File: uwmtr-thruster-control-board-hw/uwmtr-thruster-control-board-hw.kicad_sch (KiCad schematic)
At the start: 16 parts, among them J1 Conn_01x13_Pin, J2 691137710003, J3 691137710002, U1 TI_MCF8316A

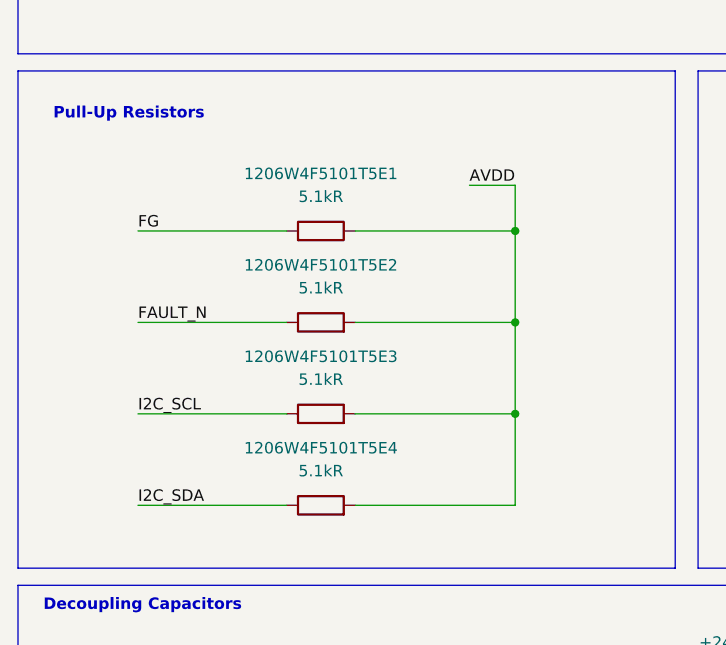
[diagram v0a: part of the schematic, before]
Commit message: Switching resistors to JLCPCB assembly non-extended parts.
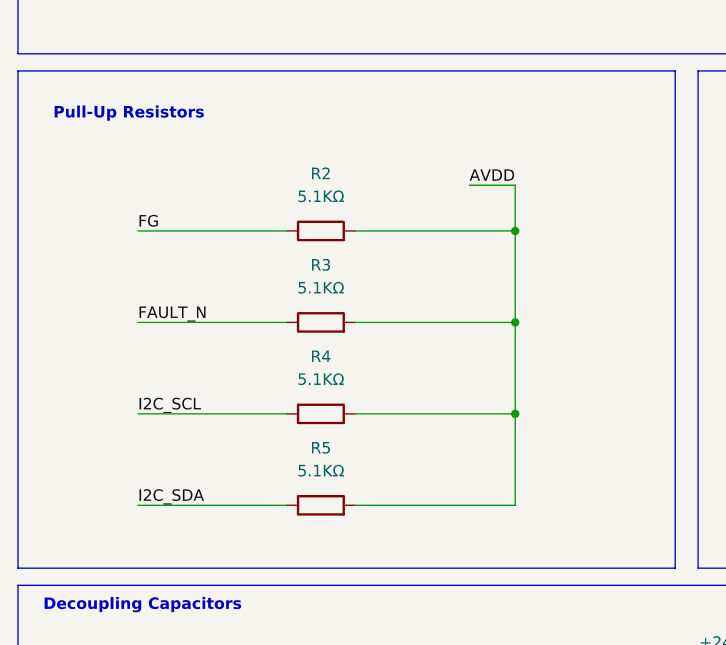
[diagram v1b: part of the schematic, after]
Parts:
- removed 1206W4F5101T5E1, 1206W4F5101T5E2, 1206W4F5101T5E3, 1206W4F5101T5E4: 5.1kR, Resistor_SMD:R_1206_3216Metric, symbol uwmtr-thruster-control-board-hw-custom-symbols:1206W4F5101T5E
- added R2, R3, R4, R5: 5.1KΩ, Resistor_SMD:R_0603_1608Metric, symbol Device:R
- R1: footprint Resistor_THT:R_Axial_DIN0207_L6.3mm_D2.5mm_P10.16mm_Horizontal -> Resistor_SMD:R_1206_3216Metric; JLCPCB Part # (none) -> C17958; MFR.Part # (none) -> 1206W4F220JT5E
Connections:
- net AVDD: now also R2.2, R3.2, R4.2, R5.2
- net FAULT_N: now also R3.1
- net FG: now also R2.1
- net I2C_SCL: now also R4.1
- net I2C_SDA: now also R5.1

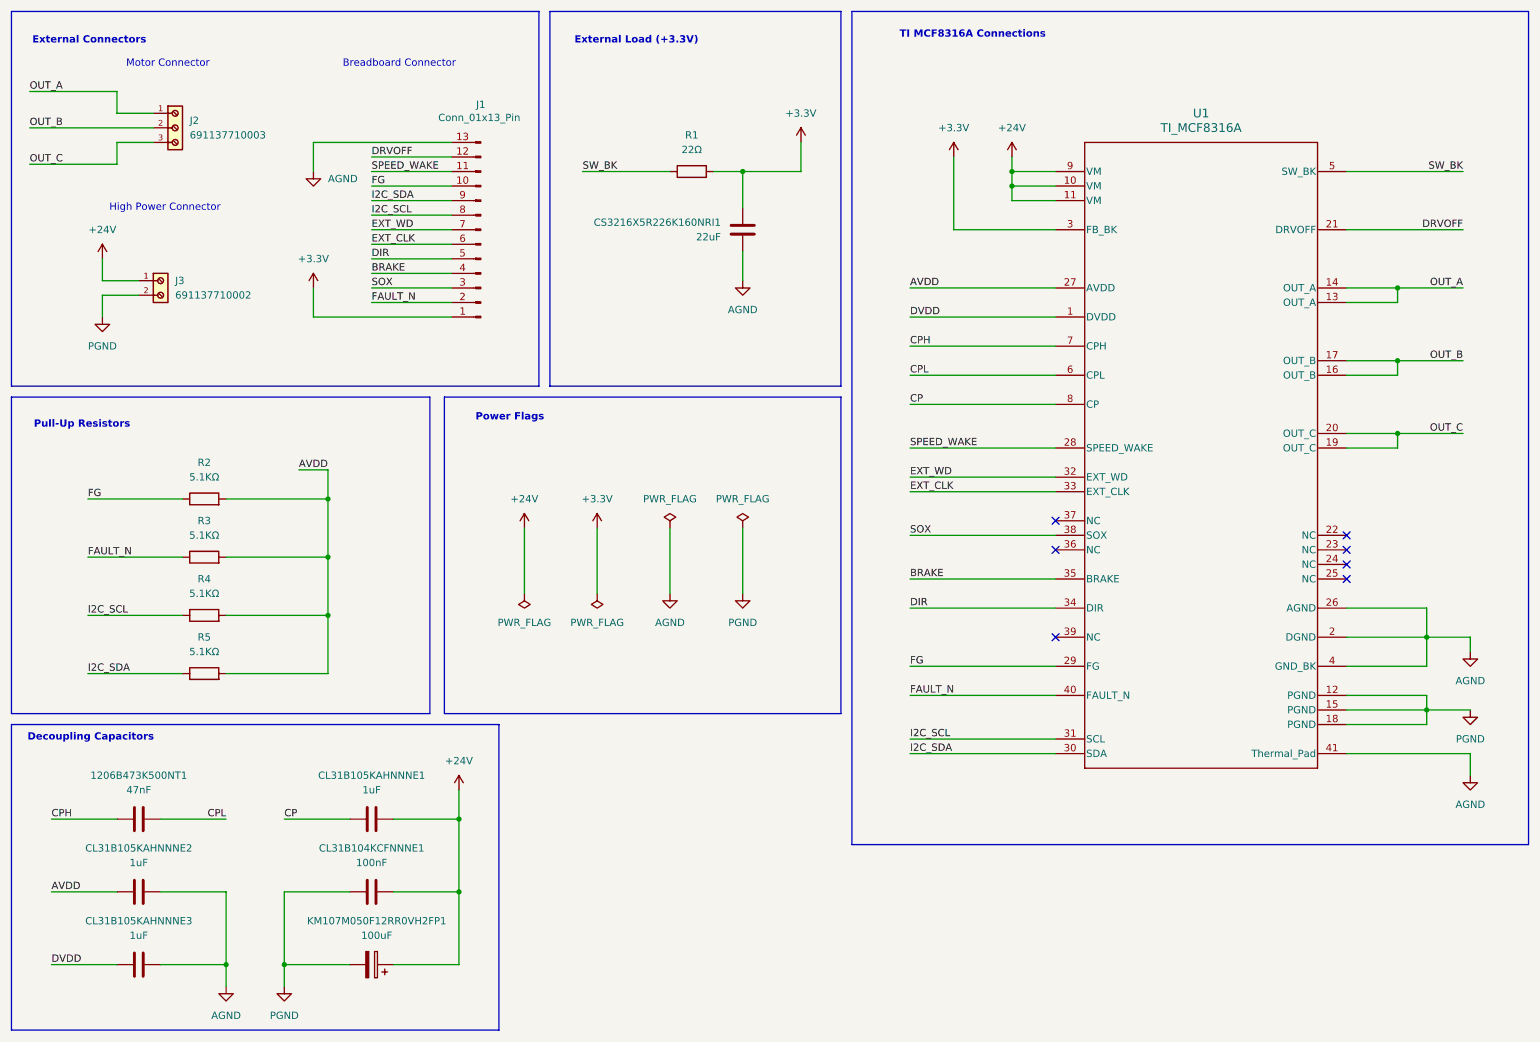
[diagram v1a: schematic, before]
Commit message: Switching components to non-extended library components where applicable and adding labels.
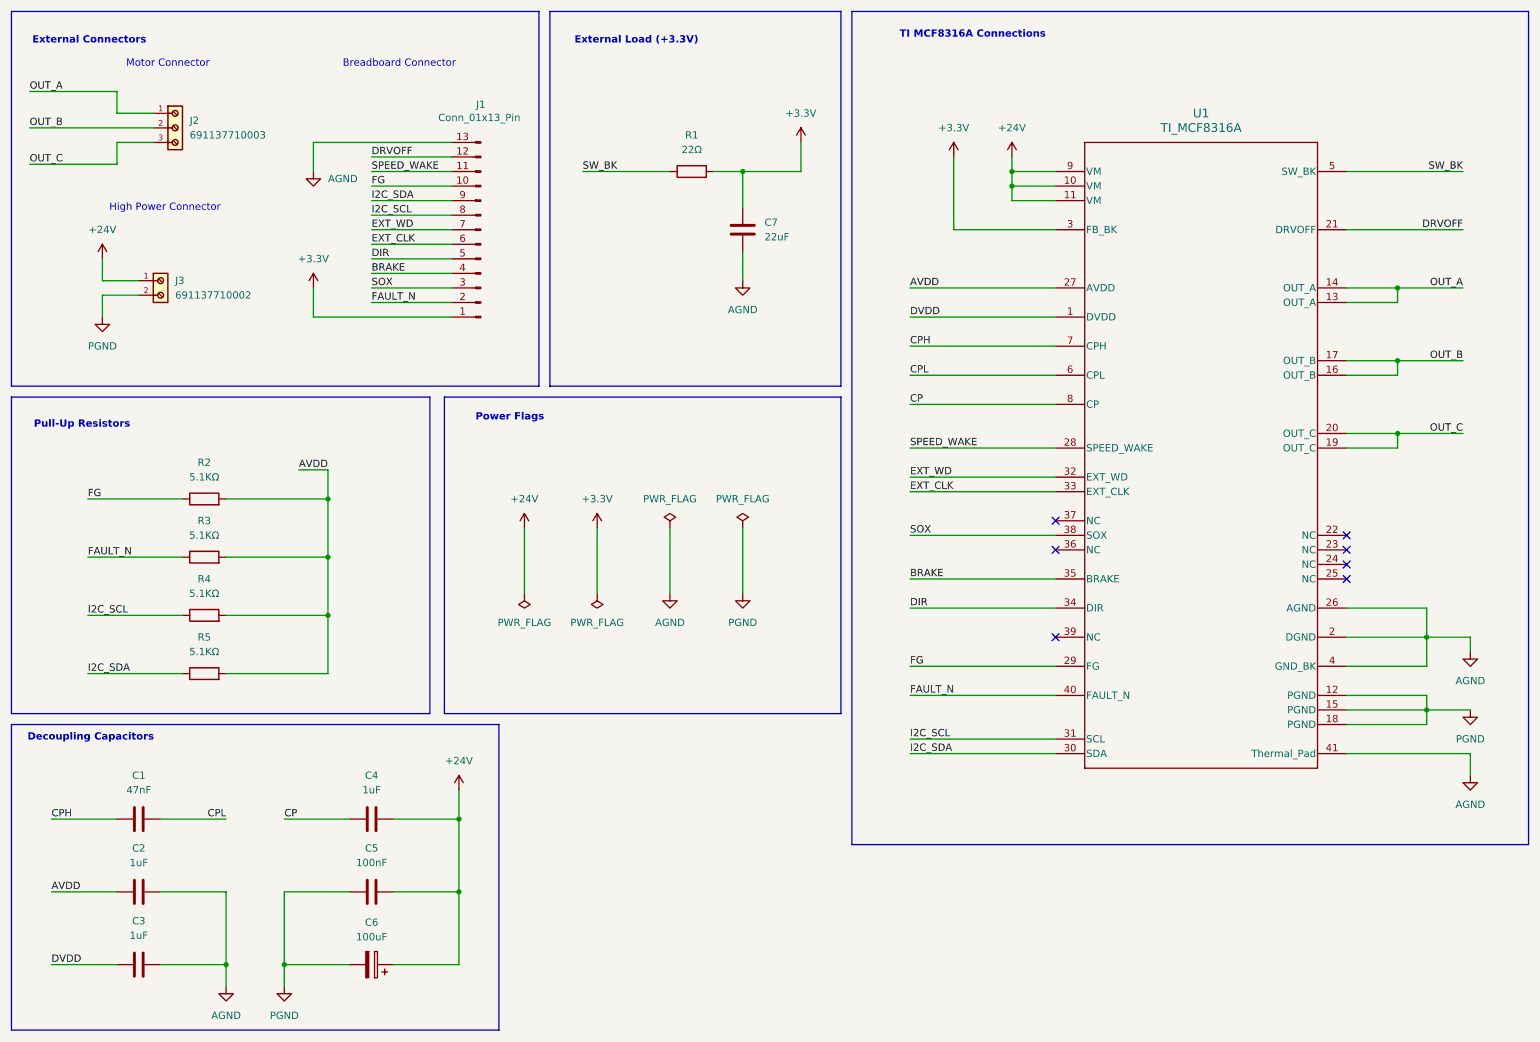
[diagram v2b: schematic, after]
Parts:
- removed 1206B473K500NT1: 47nF, Capacitor_SMD:C_1206_3216Metric, symbol uwmtr-thruster-control-board-hw-custom-symbols:1206B473K500NT
- removed CL31B104KCFNNNE1: 100nF, Capacitor_SMD:C_1206_3216Metric, symbol uwmtr-thruster-control-board-hw-custom-symbols:CL31B104KCFNNNE
- removed CL31B105KAHNNNE1, CL31B105KAHNNNE2, CL31B105KAHNNNE3: 1uF, Capacitor_SMD:C_1206_3216Metric, symbol uwmtr-thruster-control-board-hw-custom-symbols:CL31B105KAHNNNE
- removed CS3216X5R226K160NRI1: 22uF, Capacitor_SMD:C_1206_3216Metric, symbol uwmtr-thruster-control-board-hw-custom-symbols:CS3216X5R226K160NRI
- added C1: 47nF, Capacitor_SMD:C_0603_1608Metric, symbol Device:C
- added C2, C3, C4: 1uF, Capacitor_SMD:C_0603_1608Metric, symbol Device:C
- added C5: 100nF, Capacitor_SMD:C_0603_1608Metric, symbol Device:C
- added C7: 22uF, Capacitor_SMD:C_0603_1608Metric, symbol Device:C
- renumbered KM107M050F12RR0VH2FP1 to C6
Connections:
- net +24V: now also C4.2, C5.2
- net +3.3V: now also C7.2
- net AGND: now also C2.2, C3.2, C7.1
- net AVDD: now also C2.1
- net CP: now also C4.1
- net CPH: now also C1.1
- net CPL: now also C1.2
- net DVDD: now also C3.1
- net PGND: now also C5.1
